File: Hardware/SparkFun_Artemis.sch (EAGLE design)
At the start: 75 parts, among them J1 PAD.4X.6, J10 PAD.4X.6, J11 PAD.4X.6, J12 PAD.4X.6, J13 PAD.4X.6, J14 PAD.4X.6, J15 PAD.4X.6, J16 PAD.4X.6, J17 PAD.4X.6, J18 PAD.4X.6, J19 PAD.4X.6, J2 PAD.4X.6, J20 PAD.4X.6, J21 PAD.4X.6, J22 PAD.4X.6, J23 PAD.4X.6, J24 PAD.4X.6, J25 PAD.4X.6, J26 PAD.4X.6, J27 PAD.4X.6, J28 PAD.4X.6, J29 PAD.4X.6, J3 PAD.4X.6, J30 PAD.4X.6, J31 PAD.4X.6, J32 PAD.4X.6, J34 PAD.4X.6, J35 PAD.4X.6, J36 PAD.4X.6, J37 PAD.4X.6, J38 PAD.4X.6, J39 PAD.4X.6, J4 PAD.4X.6, J40 PAD.4X.6, J41 PAD.4X.6, J42 PAD.4X.6, J43 PAD.4X.6, J44 PAD.4X.6, J45 PAD.4X.6, J46 PAD.35X.35, J47 PAD.4X.6, J48 PAD.4X.6, J49 PAD.4X.6, J5 PAD.4X.6, J6 PAD.4X.6, J7 PAD.4X.6, J8 PAD.4X.6, J9 PAD.4X.6, U1 AMBIQ-APOLLO3KBR, Y1 32MHz

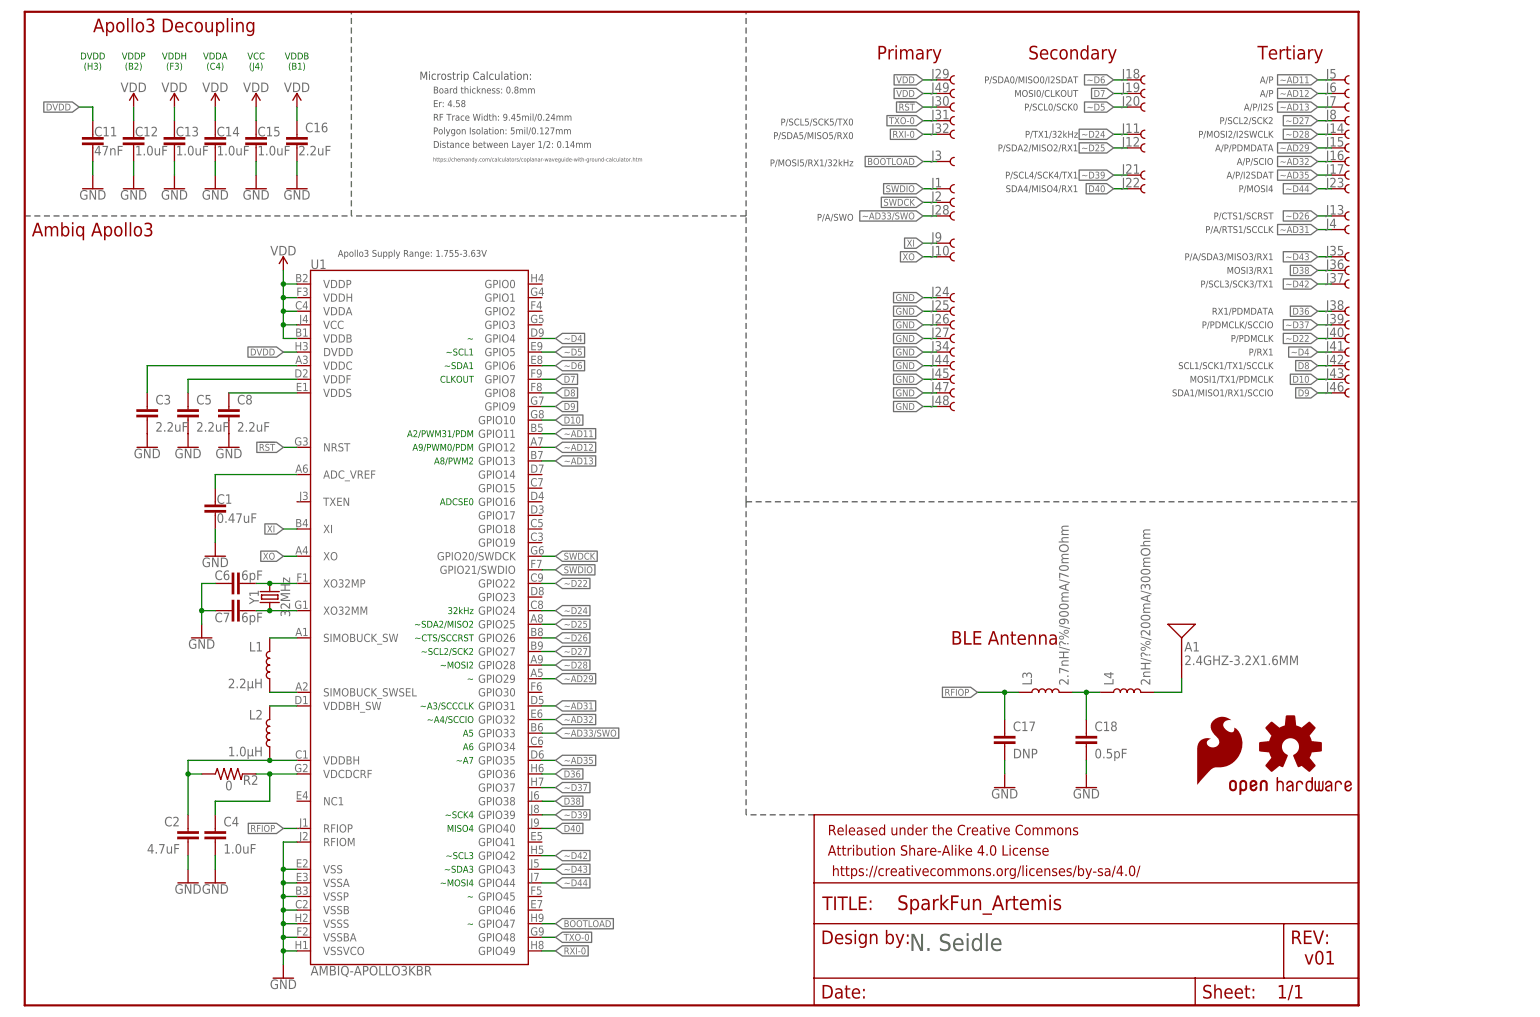
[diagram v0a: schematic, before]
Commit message: Changing RF trace width to 11.55mil
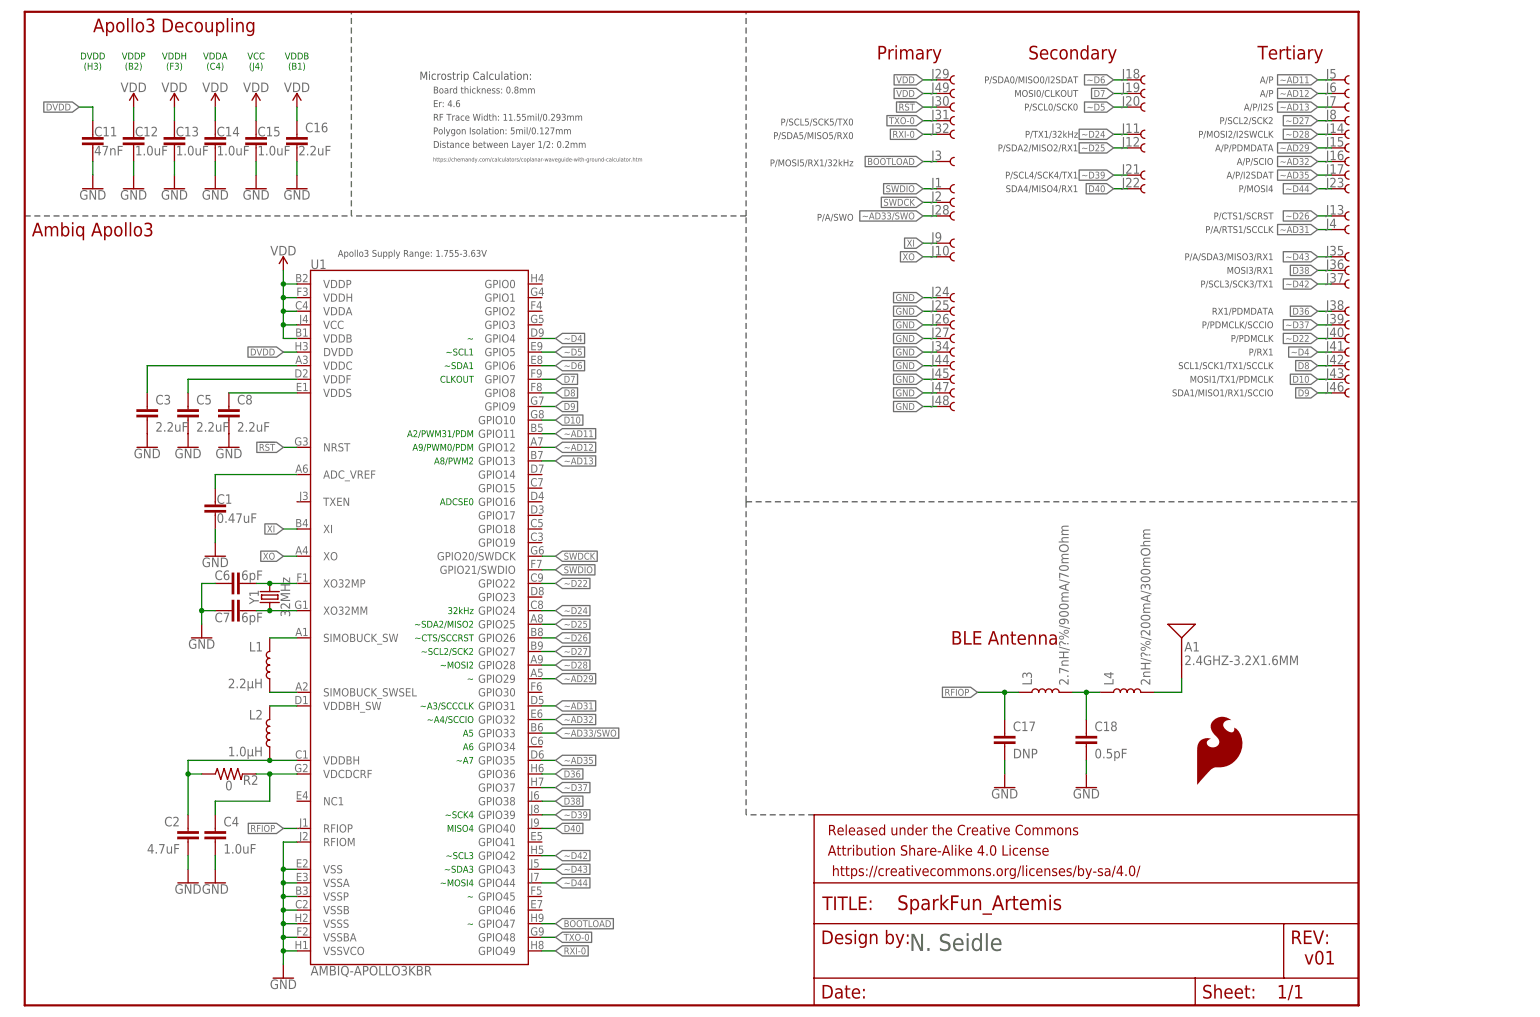
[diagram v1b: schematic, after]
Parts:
- removed LOGO2: OSHW-LOGOS, SparkFun-Aesthetics:OSHW-LOGOS
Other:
- note added: "Distance between Layer 1/2: 0.2mm"
- note added: "Er: 4.6"
- note added: "RF Trace Width: 11.55mil/0.293mm"
- note removed: "Distance between Layer 1/2: 0.14mm"
- note removed: "Er: 4.58"
- note removed: "RF Trace Width: 9.45mil/0.24mm"
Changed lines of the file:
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@@
 <part name="J44" library="Module-Pads" deviceset="PAD" device=".4X.6"/>
 <part name="LOGO1" library="SparkFun-Aesthetics" deviceset="SFE_LOGO_FLAME" device=".05_INCH_INTERNAL"/>
-<part name="LOGO2" library="SparkFun-Aesthetics" deviceset="OSHW-LOGO" device="S" value="OSHW-LOGOS"/>
 <part name="J46" library="Module-Pads" deviceset="PAD" device=".35X.35" value="PAD.35X.35"/>
 <part name="J45" library="Module-Pads" deviceset="PAD" device=".4X.6"/>
@@
 <text x="83.82" y="124.46" size="1.27" layer="91" align="center-right">~</text>
 <text x="165.1" y="10.16" size="3.175" layer="97" ratio="15">N. Seidle</text>
-<text x="76.2" y="160.02" size="1.27" layer="97">Distance between Layer 1/2: 0.14mm</text>
+<text x="76.2" y="160.02" size="1.27" layer="97">Distance between Layer 1/2: 0.2mm</text>
 <text x="73.66" y="172.72" size="1.524" layer="97" ratio="15">Microstrip Calculation:</text>
 <text x="76.2" y="170.18" size="1.27" layer="97">Board thickness: 0.8mm</text>
-<text x="76.2" y="167.64" size="1.27" layer="97">Er: 4.58</text>
-<text x="76.2" y="165.1" size="1.27" layer="97">RF Trace Width: 9.45mil/0.24mm</text>
+<text x="76.2" y="167.64" size="1.27" layer="97">Er: 4.6</text>
+<text x="76.2" y="165.1" size="1.27" layer="97">RF Trace Width: 11.55mil/0.293mm</text>
 <text x="76.2" y="162.56" size="1.27" layer="97">Polygon Isolation: 5mil/0.127mm</text>
 <text x="76.2" y="157.48" size="0.762" layer="97">https://chemandy.com/calculators/coplanar-waveguide-with-ground-calculator.htm</text>
@@
 </instance>
 <instance part="LOGO1" gate="G$1" x="218.44" y="40.64" smashed="yes"/>
-<instance part="LOGO2" gate="G$1" x="236.22" y="48.26" smashed="yes"/>
 <instance part="J46" gate="G$1" x="243.84" y="114.3" smashed="yes">
 <attribute name="NAME" x="242.824" y="114.554" size="1.778" layer="95" font="vector"/>

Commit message: Change chip antenna. Fixed shield running into trace. Post design review.
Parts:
- A1: device SparkFun-RF:ANTENNA-2.4GHZ-3.2X1.6MM-REDUCED -> SparkFun-RF:ANTENNA2.4GHZ-8.0X1.0MM
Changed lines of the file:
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@@
 <grid distance="0.1" unitdist="inch" unit="inch" style="lines" multiple="1" display="no" altdistance="0.01" altunitdist="inch" altunit="inch"/>
 <layers>
-<layer number="1" name="Top" color="4" fill="1" visible="no" active="no"/>
-<layer number="2" name="Route2" color="22" fill="3" visible="no" active="no"/>
-<layer number="3" name="Route3" color="4" fill="3" visible="no" active="no"/>
-<layer number="4" name="Route4" color="1" fill="4" visible="no" active="no"/>
-<layer number="5" name="Route5" color="4" fill="4" visible="no" active="no"/>
-<layer number="6" name="Route6" color="1" fill="8" visible="no" active="no"/>
-<layer number="7" name="Route7" color="4" fill="8" visible="no" active="no"/>
-<layer number="8" name="Route8" color="1" fill="2" visible="no" active="no"/>
-<layer number="9" name="Route9" color="4" fill="2" visible="no" active="no"/>
-<layer number="10" name="Route10" color="1" fill="7" visible="no" active="no"/>
-<layer number="11" name="Route11" color="4" fill="7" visible="no" active="no"/>
-<layer number="12" name="Route12" color="1" fill="5" visible="no" active="no"/>
-<layer number="13" name="Route13" color="4" fill="5" visible="no" active="no"/>
-<layer number="14" name="Route14" color="1" fill="6" visible="no" active="no"/>
-<layer number="15" name="Route15" color="14" fill="6" visible="no" active="no"/>
-<layer number="16" name="Bottom" color="1" fill="1" visible="no" active="no"/>
-<layer number="17" name="Pads" color="2" fill="1" visible="no" active="no"/>
-<layer number="18" name="Vias" color="2" fill="1" visible="no" active="no"/>
-<layer number="19" name="Unrouted" color="6" fill="1" visible="no" active="no"/>
-<layer number="20" name="Dimension" color="24" fill="1" visible="no" active="no"/>
-<layer number="21" name="tPlace" color="16" fill="1" visible="no" active="no"/>
-<layer number="22" name="bPlace" color="14" fill="1" visible="no" active="no"/>
-<layer number="23" name="tOrigins" color="15" fill="1" visible="no" active="no"/>
-<layer number="24" name="bOrigins" color="15" fill="1" visible="no" active="no"/>
-<layer number="25" name="tNames" color="7" fill="1" visible="no" active="no"/>
-<layer number="26" name="bNames" color="7" fill="1" visible="no" active="no"/>
-<layer number="27" name="tValues" color="7" fill="1" visible="no" active="no"/>
-<layer number="28" name="bValues" color="7" fill="1" visible="no" active="no"/>
+<layer number="1" name="Top" color="4" fill="1" visible="yes" active="no"/>
+<layer number="2" name="Route2" color="22" fill="3" visible="yes" active="no"/>
+<layer number="3" name="Route3" color="4" fill="3" visible="yes" active="no"/>
+<layer number="4" name="Route4" color="1" fill="4" visible="yes" active="no"/>
+<layer number="5" name="Route5" color="4" fill="4" visible="yes" active="no"/>
+<layer number="6" name="Route6" color="1" fill="8" visible="yes" active="no"/>
+<layer number="7" name="Route7" color="4" fill="8" visible="yes" active="no"/>
+<layer number="8" name="Route8" color="1" fill="2" visible="yes" active="no"/>
+<layer number="9" name="Route9" color="4" fill="2" visible="yes" active="no"/>
+<layer number="10" name="Route10" color="1" fill="7" visible="yes" active="no"/>
+<layer number="11" name="Route11" color="4" fill="7" visible="yes" active="no"/>
+<layer number="12" name="Route12" color="1" fill="5" visible="yes" active="no"/>
+<layer number="13" name="Route13" color="4" fill="5" visible="yes" active="no"/>
+<layer number="14" name="Route14" color="1" fill="6" visible="yes" active="no"/>
+<layer number="15" name="Route15" color="14" fill="6" visible="yes" active="no"/>
+<layer number="16" name="Bottom" color="1" fill="1" visible="yes" active="no"/>
+<layer number="17" name="Pads" color="2" fill="1" visible="yes" active="no"/>
+<layer number="18" name="Vias" color="2" fill="1" visible="yes" active="no"/>
+<layer number="19" name="Unrouted" color="6" fill="1" visible="yes" active="no"/>
+<layer number="20" name="Dimension" color="24" fill="1" visible="yes" active="no"/>
+<layer number="21" name="tPlace" color="16" fill="1" visible="yes" active="no"/>
+<layer number="22" name="bPlace" color="14" fill="1" visible="yes" active="no"/>
+<layer number="23" name="tOrigins" color="15" fill="1" visible="yes" active="no"/>
+<layer number="24" name="bOrigins" color="15" fill="1" visible="yes" active="no"/>
+<layer number="25" name="tNames" color="7" fill="1" visible="yes" active="no"/>
+<layer number="26" name="bNames" color="7" fill="1" visible="yes" active="no"/>
+<layer number="27" name="tValues" color="7" fill="1" visible="yes" active="no"/>
+<layer number="28" name="bValues" color="7" fill="1" visible="yes" active="no"/>
 <layer number="29" name="tStop" color="7" fill="3" visible="no" active="no"/>
 <layer number="30" name="bStop" color="7" fill="6" visible="no" active="no"/>
@@
 <layer number="35" name="tGlue" color="7" fill="4" visible="no" active="no"/>
 <layer number="36" name="bGlue" color="7" fill="5" visible="no" active="no"/>
-<layer number="37" name="tTest" color="7" fill="1" visible="no" active="no"/>
-<layer number="38" name="bTest" color="7" fill="1" visible="no" active="no"/>
+<layer number="37" name="tTest" color="7" fill="1" visible="yes" active="no"/>
+<layer number="38" name="bTest" color="7" fill="1" visible="yes" active="no"/>
 <layer number="39" name="tKeepout" color="4" fill="11" visible="no" active="no"/>
 <layer number="40" name="bKeepout" color="1" fill="11" visible="no" active="no"/>
@@
 <layer number="44" name="Drills" color="7" fill="1" visible="no" active="no"/>
 <layer number="45" name="Holes" color="7" fill="1" visible="no" active="no"/>
-<layer number="46" name="Milling" color="3" fill="1" visible="no" active="no"/>
-<layer number="47" name="Measures" color="7" fill="1" visible="no" active="no"/>
-<layer number="48" name="Document" color="63" fill="1" visible="no" active="no"/>
-<layer number="49" name="Reference" color="7" fill="1" visible="no" active="no"/>
-<layer number="50" name="dxf" color="47" fill="1" visible="no" active="no"/>
-<layer number="51" name="tDocu" color="6" fill="1" visible="no" active="no"/>
-<layer number="52" name="bDocu" color="7" fill="1" visible="no" active="no"/>
-<layer number="53" name="tGND_GNDA" color="7" fill="9" visible="no" active="no"/>
-<layer number="54" name="bGND_GNDA" color="1" fill="9" visible="no" active="no"/>
-<layer number="56" name="wert" color="7" fill="1" visible="no" active="no"/>
-<layer number="57" name="tCAD" color="7" fill="1" visible="no" active="no"/>
-<layer number="59" name="tCarbon" color="7" fill="1" visible="no" active="no"/>
-<layer number="60" name="bCarbon" color="7" fill="1" visible="no" active="no"/>
+<layer number="46" name="Milling" color="12" fill="1" visible="yes" active="no"/>
+<layer number="47" name="Measures" color="7" fill="1" visible="yes" active="no"/>
+<layer number="48" name="Document" color="63" fill="1" visible="yes" active="no"/>
+<layer number="49" name="Reference" color="7" fill="1" visible="yes" active="no"/>
+<layer number="50" name="dxf" color="47" fill="1" visible="yes" active="no"/>
+<layer number="51" name="tDocu" color="6" fill="1" visible="yes" active="no"/>
+<layer number="52" name="bDocu" color="29" fill="1" visible="yes" active="no"/>
+<layer number="53" name="tGND_GNDA" color="7" fill="9" visible="yes" active="no"/>
+<layer number="54" name="bGND_GNDA" color="1" fill="9" visible="yes" active="no"/>
+<layer number="56" name="wert" color="7" fill="1" visible="yes" active="no"/>
+<layer number="57" name="tCAD" color="7" fill="1" visible="yes" active="no"/>
+<layer number="59" name="tCarbon" color="7" fill="1" visible="yes" active="no"/>
+<layer number="60" name="bCarbon" color="7" fill="1" visible="yes" active="no"/>
 <layer number="88" name="SimResults" color="9" fill="1" visible="yes" active="yes"/>
 <layer number="89" name="SimProbes" color="9" fill="1" visible="yes" active="yes"/>
@@
 <part name="GND21" library="SparkFun-PowerSymbols" deviceset="GND" device=""/>
 <part name="GND17" library="SparkFun-PowerSymbols" deviceset="GND" device=""/>
-<part name="A1" library="SparkFun-RF" deviceset="ANTENNA" device="-2.4GHZ-3.2X1.6MM-REDUCED" value="2.4GHZ-3.2X1.6MM"/>
+<part name="A1" library="SparkFun-RF" deviceset="ANTENNA" device="2.4GHZ-8.0X1.0MM" value="2.4GHZ-3.2X1.6MM"/>
 <part name="R2" library="SparkFun-Resistors" deviceset="0OHM" device="-0402T-1/10W" value="0"/>
 <part name="SUPPLY5" library="SparkFun-PowerSymbols" deviceset="VDD" device=""/>
